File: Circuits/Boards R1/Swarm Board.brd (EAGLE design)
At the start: 63.5 x 63.5 mm, 90 parts, among them CON1 ISP(2X3), T1 NPN2N2222, T10 TEFT4300, T13 NPN2N2222, T14 NPN2N2222, T15 NPN2N2222, T16 NPN2N2222, T17 NPN2N2222, T18 NPN2N2222, T2 NPN2N2222, T3 NPN2N2222, T4 TEFT4300, T5 TEFT4300, T6 TEFT4300, T7 TEFT4300, T8 TEFT4300, T9 TEFT4300, U1 ATMEGA324P, U3 TB6552FN/FNG

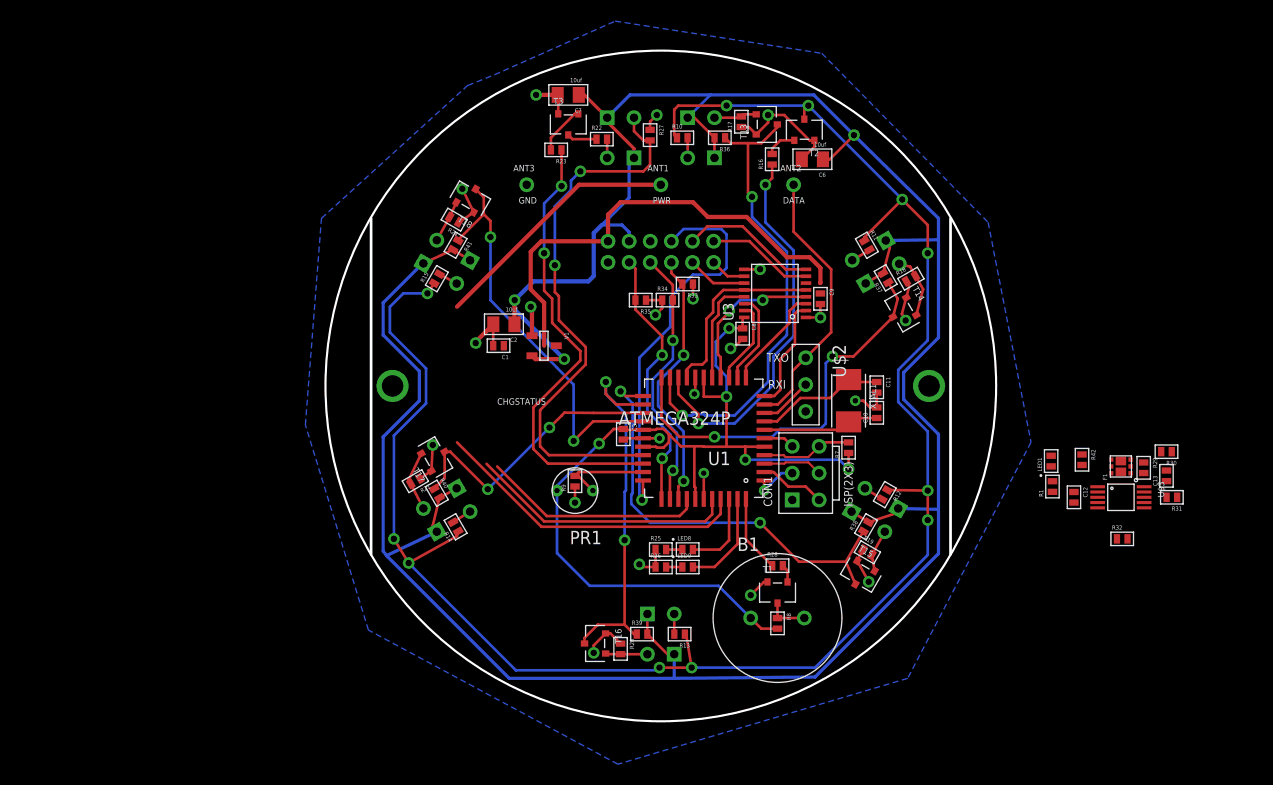
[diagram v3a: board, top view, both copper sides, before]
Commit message: started routing new charger
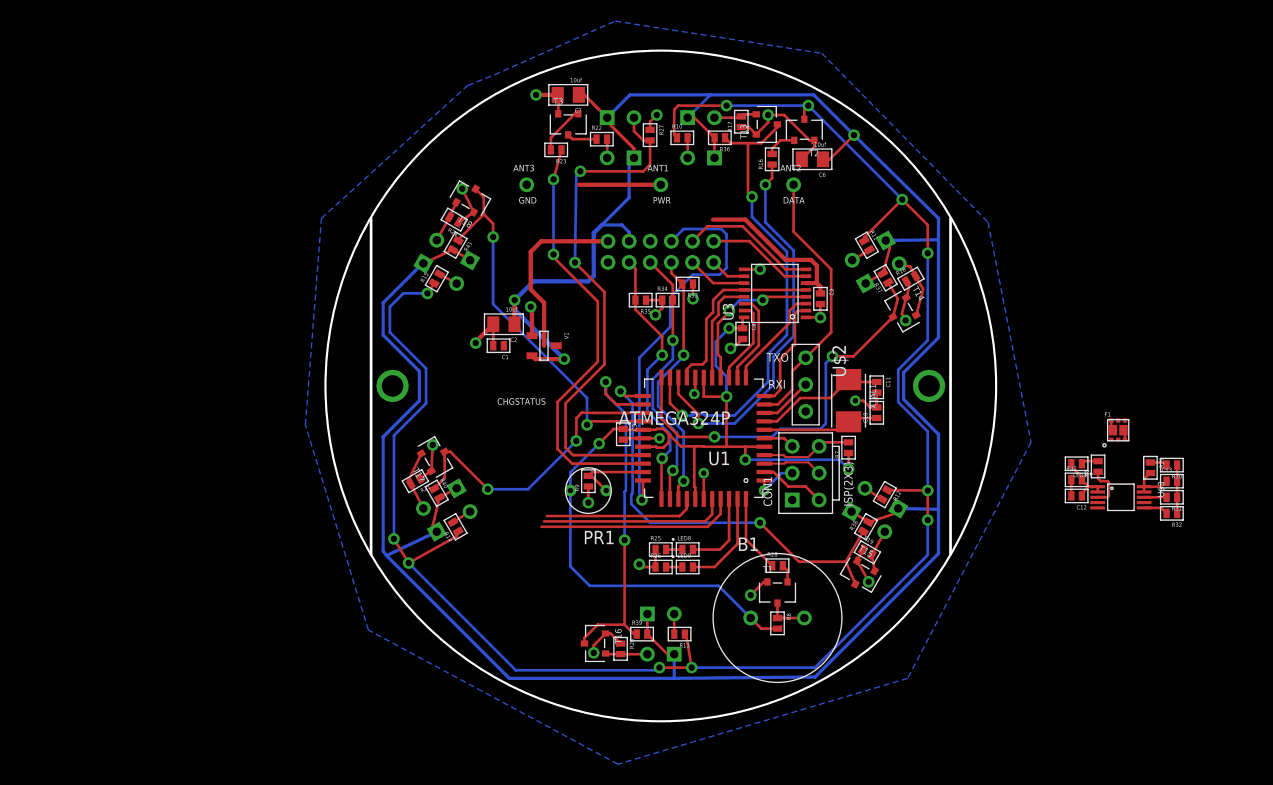
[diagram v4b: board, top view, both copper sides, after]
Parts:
- moved R32 5.28 mm to (80.1, 19.7), turned to 180 degrees
- moved R1 4.72 mm to (73.2, 24.1)
- moved F1 3.44 mm to (75.1, 27.6), turned to 0 degrees
- moved LED1 2.43 mm to (71.1, 24.4), turned to 180 degrees
- moved R42 1.97 mm to (71.1, 22.9), turned to 0 degrees
- moved R30 1.37 mm to (80.1, 24.3)
- moved PR1 1.27 mm to (24.9, 21.8)
- moved R9 1.27 mm to (24.9, 22.7)
- moved C13 0.72 mm to (80.1, 22.7), turned to 0 degrees
- moved R29 0.64 mm to (78.1, 24.0)
- moved C12 0.28 mm to (71.1, 21.3), turned to 180 degrees
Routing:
- net +VBAT: track 44.3 -> 22.5 mm
- net +VRAW: track 0.00 -> 16.6 mm
- net CHGDETECT: track 30.2 -> 18.9 mm
- net +VCHG: track 24.1 -> 13.1 mm
- net CHGSTATUS: track 25.4 -> 17.6 mm
- net GND: track 75.7 -> 81.8 mm
- net VSENSE: track 21.1 -> 16.1 mm
- net N$33: track 0.00 -> 4.20 mm
- net DISTANCERECEIVE: track 52.5 -> 49.0 mm
- net RX6: track 38.5 -> 35.6 mm
- net DISTANCELED: track 43.2 -> 40.4 mm
- net N$28: track 0.00 -> 2.34 mm
- net N$22: track 0.00 -> 2.13 mm
- net N$1: track 0.00 -> 1.63 mm
- net LIGHTSENSE: track 8.86 -> 7.59 mm
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
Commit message: 
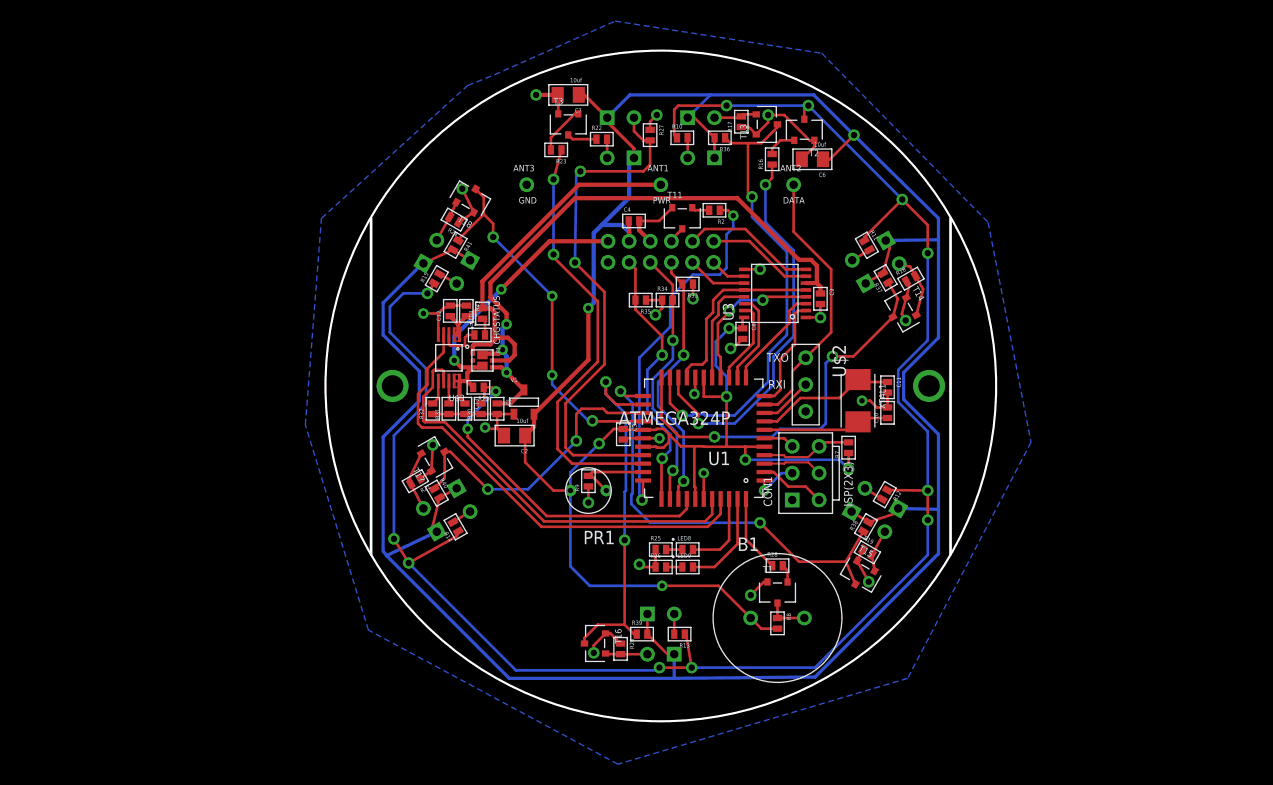
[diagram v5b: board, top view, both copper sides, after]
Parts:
- added C4, R2: (no value), Passive:0603
- added T11: NPN2N2222, Passive:SOT23
- moved R32 70.7 mm to (10.2, 29.6), turned to 90 degrees
- moved R31 69.0 mm to (11.7, 29.6), turned to 90 degrees
- moved C13 67.3 mm to (13.2, 29.6), turned to 270 degrees
- moved R30 65.6 mm to (14.7, 29.6), turned to 90 degrees
- moved U$3 65.0 mm to (11.7, 34.4), turned to 180 degrees
- moved R29 64.1 mm to (14.5, 31.6), turned to 180 degrees
- moved C12 61.8 mm to (11.8, 38.9), turned to 90 degrees
- moved F1 60.6 mm to (14.9, 34.2), turned to 270 degrees
- moved R42 60.0 mm to (13.3, 38.9), turned to 270 degrees
- moved R1 59.9 mm to (14.6, 36.6), turned to 0 degrees
- moved LED1 58.0 mm to (14.9, 38.6), turned to 90 degrees
- moved C2 10.6 mm to (17.9, 27.1)
- moved C1 5.97 mm to (16.3, 29.6), turned to 270 degrees
- moved V1 5.66 mm to (18.8, 30.2), turned to 0 degrees
- moved C10 1.02 mm to (53.2, 29.2)
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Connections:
- new net N$4: R2.2, T11.1
- new net N$7: T11.3, U$1.10
- net +3V: now also C4.1
- net CHGDETECT: now also U1.40; no longer U1.41
- net CHGSTATUS: now also U1.41; no longer U1.40
- net GND: now also C4.2, T11.2
- net IRENABLE: now also R2.1; no longer U$1.10
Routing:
- net +VRAW: track 16.6 -> 59.4 mm, vias 0 -> 3
- net +VCHG: track 13.1 -> 41.4 mm
- net CHGSTATUS: track 17.6 -> 44.0 mm
- net CHGDETECT: track 18.9 -> 40.1 mm
- net VSENSE: track 16.1 -> 33.7 mm, vias 0 -> 2
- net GND: track 81.8 -> 92.3 mm
- net +VBAT: track 22.5 -> 29.5 mm, vias 0 -> 2
- net +3V: track 358.2 -> 364.4 mm
- net N$24: track 12.5 -> 15.1 mm
- net N$23: track 11.3 -> 13.8 mm
- net IRENABLE: track 38.0 -> 35.6 mm, vias 1 -> 2
- net N$4: track 0.00 -> 1.70 mm
- net N$7: track 0.00 -> 1.60 mm
- net RX6: track 35.6 -> 35.0 mm, vias 2 -> 4
- net RX5: track 28.4 -> 29.0 mm
- added copper zone on layer 1, net +VBAT
- added copper zone on layer 1, net +VCHG

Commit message: 
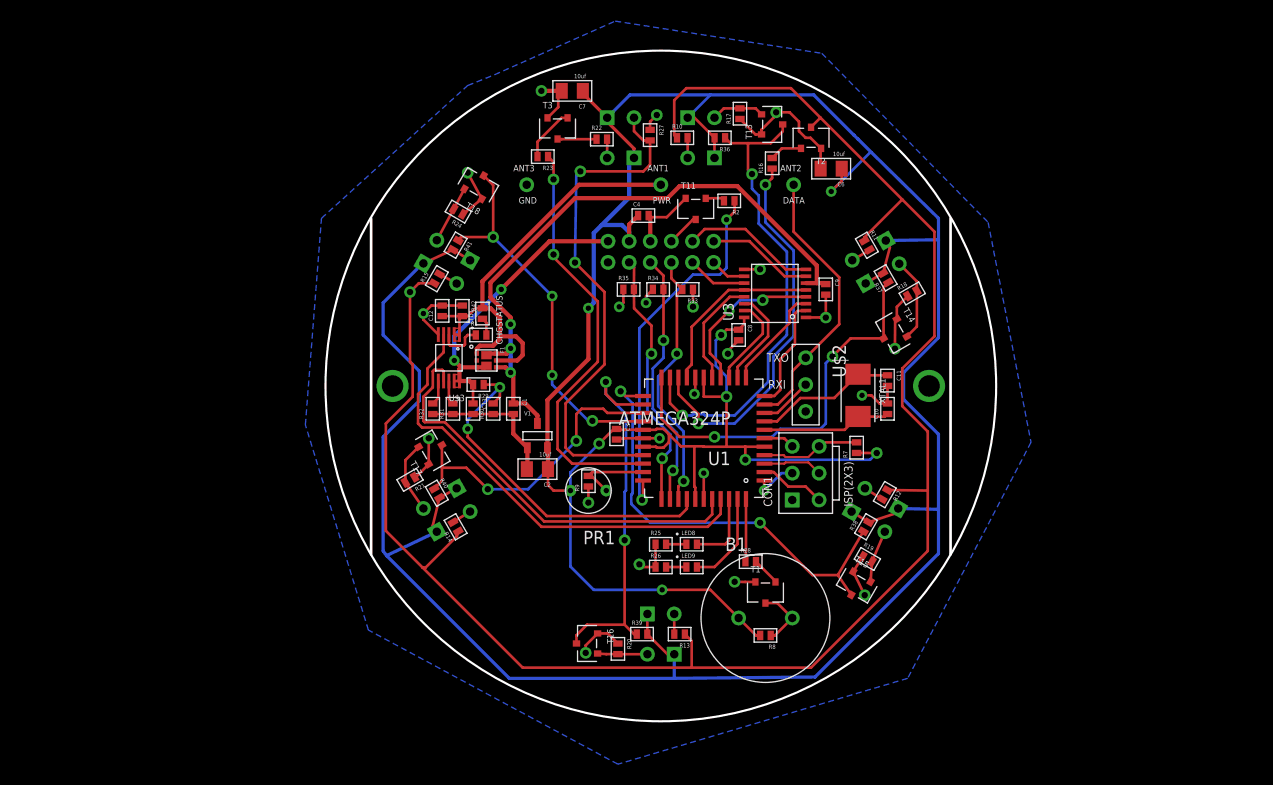
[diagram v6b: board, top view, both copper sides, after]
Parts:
- C4: value (none) -> 1uf
- R1: value (none) -> 1.5k
- R2: value (none) -> 1k
- moved C2 3.84 mm to (20.1, 23.9)
- moved V1 3.42 mm to (20.1, 27.1)
- moved R28 2.57 mm to (40.3, 15.1)
- moved T14 2.22 mm to (53.7, 36.8)
- moved C6 1.99 mm to (47.9, 52.3)
- moved R2 1.66 mm to (38.2, 49.3)
- moved R8 1.62 mm to (41.7, 8.13), turned to 180 degrees
- moved T11 1.55 mm to (35.1, 48.5)
- moved R35 1.53 mm to (28.7, 40.9), turned to 0 degrees
- moved C1 1.52 mm to (17.8, 29.6)
- moved T18 1.48 mm to (14.5, 50.8)
- moved R23 1.42 mm to (20.6, 53.5)
- moved R18 1.40 mm to (55.6, 40.5)
- moved R34 1.35 mm to (31.5, 40.9)
- moved B1 1.14 mm to (41.7, 9.78)
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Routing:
- net GND: track 92.3 -> 106.0 mm
- net +3V: track 364.4 -> 368.9 mm
- net +VCHG: track 41.4 -> 43.5 mm
- net +VRAW: track 59.4 -> 61.4 mm
- net N$38: track 6.07 -> 7.97 mm
- net N$9: track 3.96 -> 5.85 mm
- net N$10: track 175.3 -> 173.4 mm, vias 11 -> 1
- net N$24: track 15.1 -> 13.5 mm
- net N$7: track 1.60 -> 3.16 mm
- net N$23: track 13.8 -> 12.3 mm
- net N$34: track 4.04 -> 5.52 mm
- net BUZZER: track 7.34 -> 5.94 mm
- net RX3: track 41.7 -> 42.9 mm
- net N$26: track 1.73 -> 2.93 mm
- net N$35: track 5.81 -> 6.88 mm
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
